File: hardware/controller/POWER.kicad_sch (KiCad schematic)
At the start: 19 parts, among them IC1 TPS63000IDRCRQ1, J1 Conn_01x02_Pin

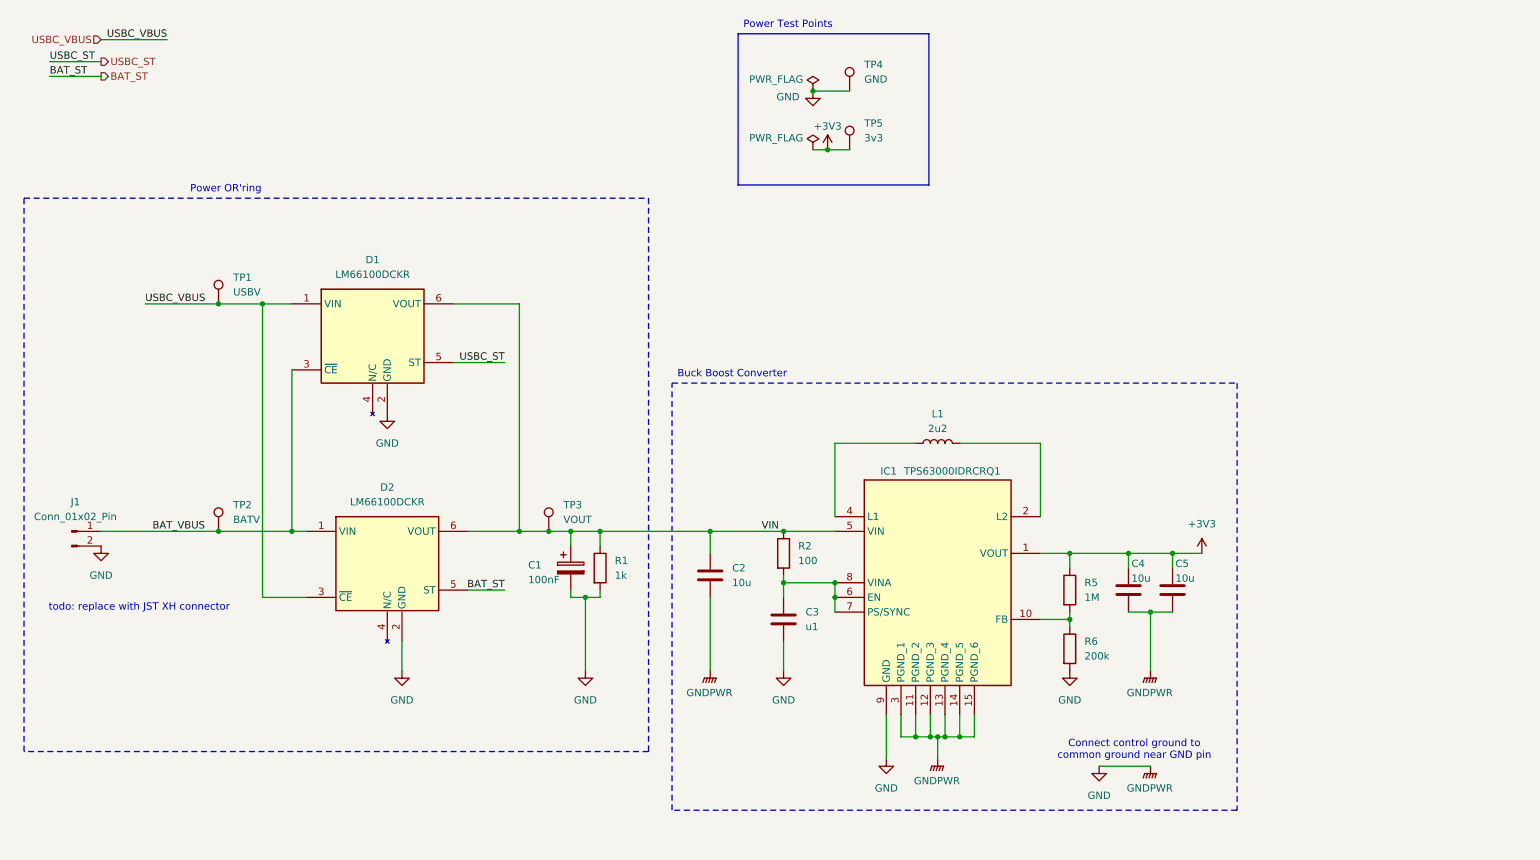
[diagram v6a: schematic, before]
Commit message: ERC good to go. grouped all components on pcb
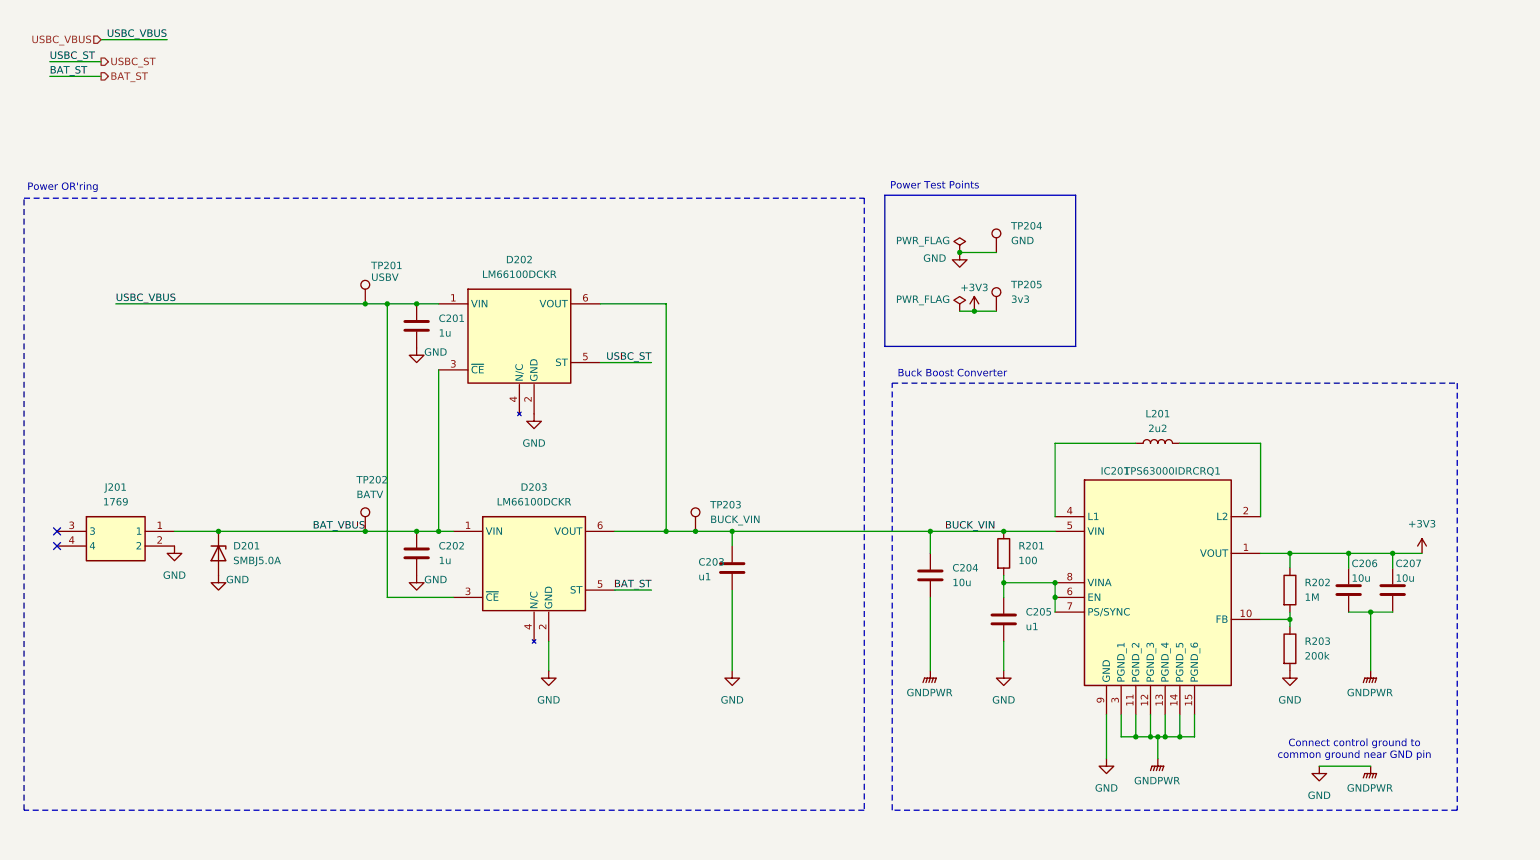
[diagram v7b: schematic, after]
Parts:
- removed C1: 100nF, symbol Device:C_Polarized
- removed J1: Conn_01x02_Pin, symbol Connector:Conn_01x02_Pin
- removed R1: 1k, RESC3116X65N, symbol Device:R
- added C201, C202: 1u, SamacSys_Parts:CAPC2012X135N, symbol Device:C
- added C203: u1, SamacSys_Parts:MAJx16, symbol Device:C
- added D201: SMBJ5.0A, SamacSys_Parts:DIOM5436X261N, symbol Device:D_Zener
- added J201: 1769, SamacSys_Parts:1769, symbol SamacSys_Parts:1769
- C204: renamed from C2; footprint CAPC1608X80N -> SamacSys_Parts:CAPC1608X80N
- C205: renamed from C3; footprint MAJx16 -> SamacSys_Parts:MAJx16
- C206: renamed from C4; footprint CAPC1608X80N -> SamacSys_Parts:CAPC1608X80N
- C207: renamed from C5; footprint CAPC1608X80N -> SamacSys_Parts:CAPC1608X80N
- D202: renamed from D1; footprint SOP65P210X110-6N -> SamacSys_Parts:SOP65P210X110-6N
- D203: renamed from D2; footprint SOP65P210X110-6N -> SamacSys_Parts:SOP65P210X110-6N
- IC201: renamed from IC1; footprint TPS63000IDRCRQ1 -> SamacSys_Parts:TPS63000IDRCRQ1
- L201: renamed from L1; footprint NRS3015T2R2MNGHV -> SamacSys_Parts:NRS3015T2R2MNGHV
- R201: renamed from R2; footprint (none) -> SamacSys_Parts:ERJP08__1206_; Height (none) -> 0.7; Manufacturer_Name (none) -> Panasonic; Manufacturer_Part_Number (none) -> ERJ-P08J101V; Mouser Part Number (none) -> 667-ERJ-P08J101V; Mouser Price/Stock (none) -> https://www.mouser.co.uk/ProductDetail/Panasonic/ERJ-P08J10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
- R202: renamed from R5; footprint (none) -> Resistor_SMD:R_0603_1608Metric; Mouser Part Number (none) -> 755-SFR03EZPJ105; Mouser Price/Stock (none) -> https://www.mouser.com/ProductDetail/ROHM-Semiconductor/SFR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
- R203: renamed from R6; footprint (none) -> SamacSys_Parts:RESC1608X55N; Height (none) -> 0.55; Manufacturer_Name (none) -> ROHM Semiconductor; Manufacturer_Part_Number (none) -> KTR03EZPJ204; Mouser Part Number (none) -> 755-KTR03EZPJ204; Mouser Price/Stock (none) -> https://www.mouser.co.uk/ProductDetail/ROHM-Semiconductor/K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
- TP203: renamed from TP3; value VOUT -> BUCK_VIN
- renumbered TP1 to TP201, TP2 to TP202, TP4 to TP204, TP5 to TP205
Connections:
- net BAT_VBUS: now also C202.1, D201.1 (K), J201.1
- net GND: now also C201.2, C202.2, C203.2, D201.2 (A), J201.2
- net USBC_VBUS: now also C201.1
- net VIN renamed BUCK_VIN
- net BUCK_VIN: now also C203.1
- no-connect marks 0 -> 2
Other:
- note removed: "todo: replace with JST XH connector"
- moved on the sheet: C204, C205, C206, C207, D202, D203, IC201, L201, R201, R202, R203, TP201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

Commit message: fixed 3d models. rounded edges of pcb
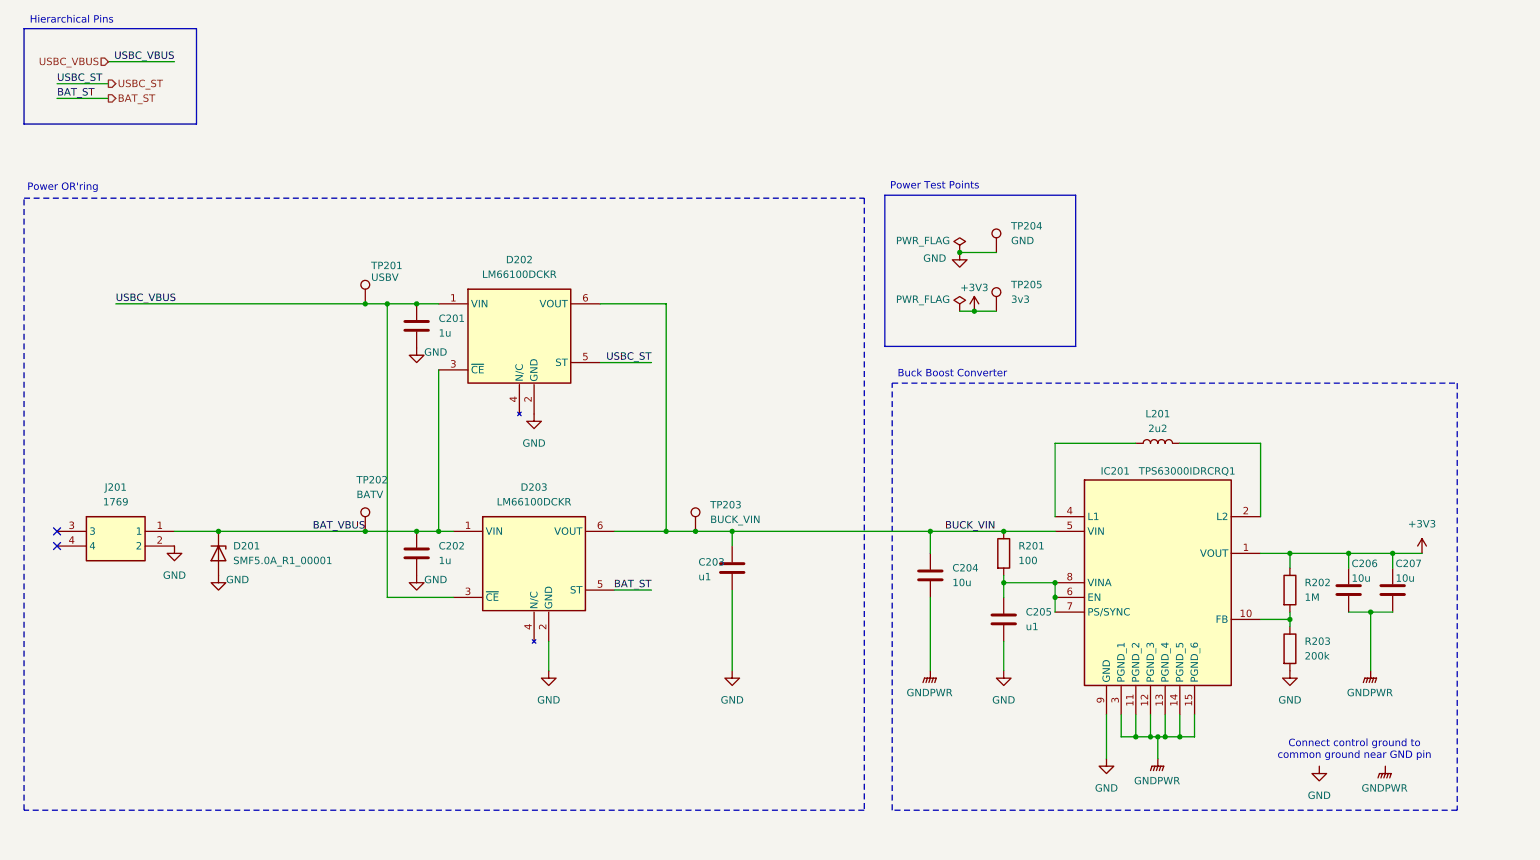
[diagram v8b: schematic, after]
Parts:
- D201: value SMBJ5.0A -> SMF5.0A_R1_00001; footprint SamacSys_Parts:DIOM5436X261N -> SMF50A_R1_00001; Height 2.61 -> 1.1; Manufacturer_Name LITTELFUSE -> PANJIT; Manufacturer_Part_Number SMBJ5.0A -> SMF5.0A_R1_00001; Mouser Part Number 576-SMBJ5.0A -> 241-SMF5.0A_R1_00001; Mouser Price/Stock https://www.mouser.co.uk/ProductDetail/Littelfuse/SMBJ5.0A?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 -> https://www.mouser.co.uk/ProductDetail/Panjit/SMF5.0A_R1_00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
- R201: footprint SamacSys_Parts:ERJP08__1206_ -> RESC1608X55N; Height 0.7 -> 0.55; Manufacturer_Name Panasonic -> ROHM Semiconductor; Manufacturer_Part_Number ERJ-P08J101V -> ESR03EZPF1000; Mouser Part Number 667-ERJ-P08J101V -> 755-ESR03EZPF1000; Mouser Price/Stock https://www.mouser.co.uk/ProductDetail/Panasonic/ERJ-P08J10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 -> https://www.mouser.co.uk/ProductDetail/ROHM-Semiconductor/E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
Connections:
- net GND: no longer C204.2, C206.2, C207.2, IC201.11 (PGND_2), IC201.12 (PGND_3), IC201.13 (PGND_4), IC201.14 (PGND_5), IC201.15 (PGND_6), IC201.3 (PGND_1)
- new net GNDPWR: C204.2, C206.2, C207.2, IC201.11 (PGND_2), IC201.12 (PGND_3), IC201.13 (PGND_4), IC201.14 (PGND_5), IC201.15 (PGND_6), IC201.3 (PGND_1)
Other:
- note added: "Hierarchical Pins"
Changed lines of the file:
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@@
 	)
 	(rectangle
+		(start 17.145 23.495)
+		(end 46.99 40.005)
+		(stroke
+			(width 0)
+			(type default)
+		)
+		(fill
+			(type none)
+		)
+	)
+	(rectangle
 		(start 166.116 52.324)
 		(end 199.136 78.486)
@@
 		)
 	)
+	(text "Hierarchical Pins"
+		(exclude_from_sim no)
+		(at 25.4 22.098 0)
+		(effects
+			(font
+				(size 1.27 1.27)
+			)
+		)
+	)
 	(junction
 		(at 181.61 72.39)
@@
 	)
 	(junction
-		(at 214.63 146.05)
+		(at 186.69 110.49)
 		(diameter 0)
 		(color 0 0 0 0)
 	)
 	(junction
-		(at 50.8 110.49)
+		(at 214.63 146.05)
 		(diameter 0)
 		(color 0 0 0 0)
@@
 	)
 	(junction
-		(at 186.69 110.49)
-		(diameter 0)
-		(color 0 0 0 0)
-	)
-	(junction
 		(at 133.35 110.49)
 		(diameter 0)
@@
 	)
 	(junction
+		(at 50.8 110.49)
+		(diameter 0)
+		(color 0 0 0 0)
+	)
+	(junction
 		(at 88.9 110.49)
 		(diameter 0)
@@
 	(wire
 		(pts
-			(xy 50.8 110.49) (xy 76.2 110.49)
+			(xy 186.69 110.49) (xy 195.58 110.49)
 		)
 		(stroke
@@
 	(wire
 		(pts
-			(xy 21.59 31.75) (xy 30.48 31.75)
+			(xy 22.86 35.56) (xy 31.75 35.56)
 		)
 		(stroke
@@
 	(wire
 		(pts
+			(xy 50.8 110.49) (xy 76.2 110.49)
+		)
+		(stroke
+			(width 0)
+			(type default)
+		)
+	)
+	(wire
+		(pts
 			(xy 236.22 114.3) (xy 231.14 114.3)
 		)
@@
 	(wire
 		(pts
-			(xy 21.59 29.21) (xy 30.48 29.21)
+			(xy 22.86 33.02) (xy 31.75 33.02)
 		)
 		(stroke
@@
 	(wire
 		(pts
-			(xy 241.3 151.13) (xy 250.19 151.13)
-		)
-		(stroke
-			(width 0)
-			(type default)
-		)
-	)
-	(wire
-		(pts
 			(xy 173.99 110.49) (xy 186.69 110.49)
 		)
@@
 	(wire
 		(pts
-			(xy 186.69 110.49) (xy 195.58 110.49)
-		)
-		(stroke
-			(width 0)
-			(type default)
-		)
-	)
-	(wire
-		(pts
 			(xy 217.17 146.05) (xy 219.71 146.05)
 		)
@@
 	(wire
 		(pts
-			(xy 41.91 25.4) (xy 30.48 25.4)
+			(xy 43.18 29.21) (xy 31.75 29.21)
 		)
 		(stroke
@@
 	)
 	(label "BAT_ST"
-		(at 21.59 31.75 0)
+		(at 22.86 35.56 0)
 		(effects
 			(font
@@
 	)
 	(label "USBC_VBUS"
-		(at 41.91 25.4 180)
+		(at 43.18 29.21 180)
 		(effects
 			(font
@@
 	)
 	(label "USBC_ST"
-		(at 21.59 29.21 0)
+		(at 22.86 33.02 0)
 		(effects
 			(font
@@
 	(hierarchical_label "USBC_VBUS"
 		(shape input)
-		(at 30.48 25.4 180)
+		(at 31.75 29.21 180)
 		(effects
 			(font
@@
 	(hierarchical_label "BAT_ST"
 		(shape output)
-		(at 30.48 31.75 0)
+		(at 31.75 35.56 0)
 		(effects
 			(font
@@
 	(hierarchical_label "USBC_ST"
 		(shape output)
-		(at 30.48 29.21 0)
+		(at 31.75 33.02 0)
 		(effects
 			(font
@@
 	(symbol
 		(lib_id "power:GNDPWR")
-		(at 250.19 151.13 0)
+		(at 252.73 151.13 0)
 		(unit 1)
 		(exclude_from_sim no)
@@
 		(fields_autoplaced yes)
 		(property "Reference" "#PWR0217"
-			(at 250.19 156.21 0)
+			(at 252.73 156.21 0)
 			(effects
 				(font
@@
 		)
 		(property "Value" "GNDPWR"
-			(at 250.063 154.94 0)
+			(at 252.603 154.94 0)
 			(effects
 				(font
@@
 		)
 		(property "Footprint" ""
-			(at 250.19 152.4 0)
+			(at 252.73 152.4 0)
 			(effects
 				(font
@@
 		)
 		(property "Datasheet" ""
-			(at 250.19 152.4 0)
+			(at 252.73 152.4 0)
 			(effects
 				(font
@@
 		)
 		(property "Description" "Power symbol creates a global label with name \"GNDPWR\" , global ground"
-			(at 250.19 151.13 0)
+			(at 252.73 151.13 0)
 			(effects
 				(font
@@
 			)
 		)
-		(property "Footprint" "SamacSys_Parts:ERJP08__1206_"
+		(property "Footprint" "RESC1608X55N"
 			(at 200.66 210.49 0)
 			(effects
@@
 			)
 		)
-		(property "Datasheet" "http://industrial.panasonic.com/cdbs/www-data/pdf/RDO0000/AOA0000C331.pdf"
+		(property "Datasheet" "https://componentsearchengine.com//ESR03EZPF1000.pdf"
 			(at 200.66 310.49 0)
 			(effects
@@
 			)
 		)
-		(property "Description" "Thick Film Resistors - SMD 1206 100ohms 0.66W 5% AEC-Q200"
+		(property "Description" "Thick Film Resistors - SMD 0603 100ohm 1% Anti Surge AEC-Q200"
 			(at 186.69 114.3 0)
 			(effects
@@
 			)
 		)
-		(property "Height" "0.7"
+		(property "Height" "0.55"
 			(at 200.66 510.49 0)
 			(effects
@@
 			)
 		)
-		(property "Mouser Part Number" "667-ERJ-P08J101V"
+		(property "Mouser Part Number" "755-ESR03EZPF1000"
 			(at 200.66 610.49 0)
 			(effects
@@
 			)
 		)
-		(property "Mouser Price/Stock" "https://www.mouser.co.uk/ProductDetail/Panasonic/ERJ-P08J101V?qs=1VWA5LkbEapwjh56YeyL%252Bw%3D%3D"
+		(property "Mouser Price/Stock" "https://www.mouser.co.uk/ProductDetail/ROHM-Semiconductor/ESR03EZPF1000?qs=493kPxzlxfJdLkJZpX4ByA%3D%3D"
 			(at 200.66 710.49 0)
 			(effects
@@
 			)
 		)
-		(property "Manufacturer_Name" "Panasonic"
+		(property "Manufacturer_Name" "ROHM Semiconductor"
 			(at 200.66 810.49 0)
 			(effects
@@
 			)
 		)
-		(property "Manufacturer_Part_Number" "ERJ-P08J101V"
+		(property "Manufacturer_Part_Number" "ESR03EZPF1000"
 			(at 200.66 910.49 0)
 			(effects
@@
 			)
 		)
-		(property "Value" "SMBJ5.0A"
+		(property "Value" "SMF5.0A_R1_00001"
 			(at 53.34 115.5699 90)
 			(effects
@@
 			)
 		)
-		(property "Footprint" "SamacSys_Parts:DIOM5436X261N"
+		(property "Footprint" "SMF50A_R1_00001"
 			(at -42.85 124.46 0)
 			(effects
@@
 			)
 		)
-		(property "Datasheet" "https://www.mouser.co.uk/datasheet/2/240/Littelfuse_TVS_Diode_SMBJ_Datasheet.pdf-1108540.pdf"
+		(property "Datasheet" "https://www.mouser.in/datasheet/2/1057/SMF5.0A_SERIES-1868418.pdf"
 			(at -142.85 124.46 0)
 			(effects
@@
 			)
 		)
-		(property "Description" "Littelfuse SMBJ5.0A, Uni-Directional TVS Diode, 600W, 2-Pin DO-214AA"
+		(property "Description" "ESD Suppressors / TVS Diodes 200W,Transient Voltage Suppressors,SOD-123FL,5V,UNI"
 			(at 50.8 114.3 0)
 			(effects
@@
 			)
 		)
-		(property "Height" "2.61"
+		(property "Height" "1.1"
 			(at -342.85 124.46 0)
 			(effects
@@
 			)
 		)
-		(property "Mouser Part Number" "576-SMBJ5.0A"
+		(property "Mouser Part Number" "241-SMF5.0A_R1_00001"
 			(at -442.85 124.46 0)
 			(effects
@@
 			)
 		)
-		(property "Mouser Price/Stock" "https://www.mouser.co.uk/ProductDetail/Littelfuse/SMBJ5.0A?qs=JJML70Qc14t9tktzNr1oMQ%3D%3D"
+		(property "Mouser Price/Stock" "https://www.mouser.co.uk/ProductDetail/Panjit/SMF5.0A_R1_00001?qs=sPbYRqrBIVlx%2FHVv%252BUyL%252BQ%3D%3D"
 			(at -542.85 124.46 0)
 			(effects
@@
 			)
 		)
-		(property "Manufacturer_Name" "LITTELFUSE"
+		(property "Manufacturer_Name" "PANJIT"
 			(at -642.85 124.46 0)
 			(effects
@@
 			)
 		)
-		(property "Manufacturer_Part_Number" "SMBJ5.0A"
+		(property "Manufacturer_Part_Number" "SMF5.0A_R1_00001"
 			(at -742.85 124.46 0)
 			(effects
@@
 		)
 		(property "Value" "TPS63000IDRCRQ1"
-			(at 207.518 100.076 0)
+			(at 210.058 100.076 0)
 			(effects
 				(font
